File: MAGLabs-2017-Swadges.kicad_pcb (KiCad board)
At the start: 2 copper layers, 70 x 120 mm, 34 parts, among them J1 LCD Screen, J2 Valve Magic, J3 Program, U1 ESP12E

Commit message: Update Swadges design
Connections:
- D2 pad 1: Net-(D2-Pad1) -> (no net)
- D7 pad 2: Net-(D7-Pad2) -> (no net)
- D8 pad 2: Net-(D8-Pad2) -> (no net)
- R2 pad 2: Net-(R2-Pad2) -> (no net)
- R3 pad 2: Net-(R3-Pad2) -> (no net)
- U1 pad 10: Net-(U1-Pad10) -> (no net)
- U1 pad 11: Net-(U1-Pad11) -> (no net)
- U1 pad 12: Net-(U1-Pad12) -> (no net)
- U1 pad 13: Net-(U1-Pad13) -> (no net)
- U1 pad 14: Net-(U1-Pad14) -> (no net)
- U1 pad 9: Net-(U1-Pad9) -> (no net)
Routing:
- net GND: track 0.00 -> 126.5 mm, vias 0 -> 15
- net +3V3: track 307.6 -> 309.2 mm, vias 0 -> 2
- net Net-(BT1-Pad2): track 81.6 -> 81.7 mm, vias 0 -> 4

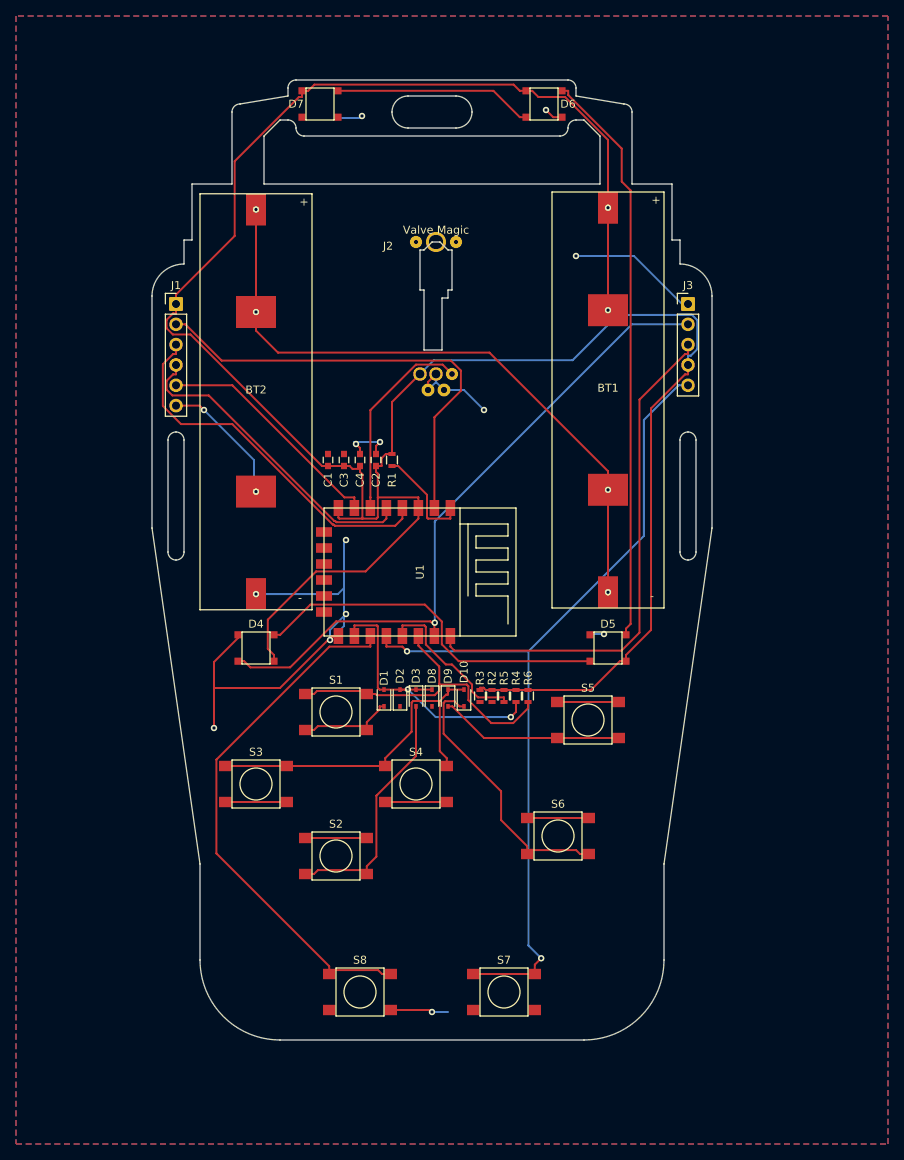
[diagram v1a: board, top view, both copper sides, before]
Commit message: Cleanup outputs
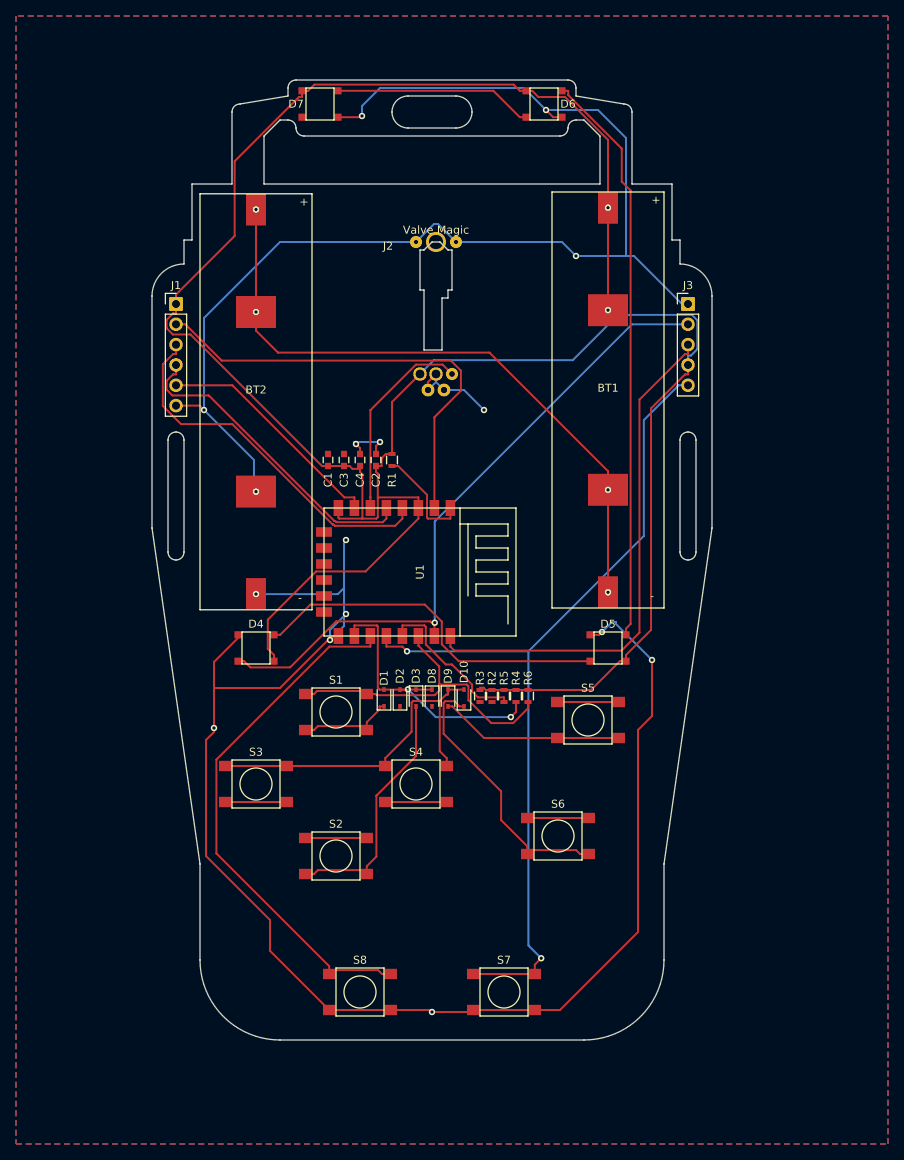
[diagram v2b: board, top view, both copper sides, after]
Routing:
- net GND: track 126.5 -> 366.9 mm, vias 15 -> 16
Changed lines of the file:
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@@
     (thickness 1.6)
     (drawings 74)
-    (tracks 383)
+    (tracks 419)
     (zones 0)
     (modules 34)
@@
   (segment (start 168 70.62) (end 168 71.7953) (width 0.25) (layer F.Cu) (net 2))
   (segment (start 160.25 107.65) (end 160.25 106.8747) (width 0.25) (layer F.Cu) (net 2))
-  (segment (start 152.25 39.65) (end 151.15 39.65) (width 0.25) (layer F.Cu) (net 3) (status 400000))
+  (segment (start 107.5 76.25) (end 107.5 64.75) (width 0.25) (layer B.Cu) (net 3))
+  (segment (start 117 55.25) (end 134 55.25) (width 0.25) (layer B.Cu) (net 3) (status 800000))
+  (segment (start 107.5 64.75) (end 117 55.25) (width 0.25) (layer B.Cu) (net 3))
+  (segment (start 139 55.25) (end 136.75 53) (width 0.25) (layer B.Cu) (net 3) (status 400000))
+  (segment (start 136.75 53) (end 136.25 53) (width 0.25) (layer B.Cu) (net 3))
+  (segment (start 136.25 53) (end 134 55.25) (width 0.25) (layer B.Cu) (net 3) (status 800000))
+  (segment (start 139 55.25) (end 152.25 55.25) (width 0.25) (layer B.Cu) (net 3) (status 400000))
+  (via (at 154 57) (size 0.8) (drill 0.4) (layers F.Cu B.Cu) (net 3))
+  (segment (start 154 57) (end 160.25 57) (width 0.25) (layer B.Cu) (net 3))
+  (segment (start 152.25 55.25) (end 154 57) (width 0.25) (layer B.Cu) (net 3))
+  (segment (start 150.25 38.75) (end 156.75 38.75) (width 0.25) (layer B.Cu) (net 3))
+  (segment (start 160.25 42.25) (end 160.25 57) (width 0.25) (layer B.Cu) (net 3))
+  (segment (start 156.75 38.75) (end 160.25 42.25) (width 0.25) (layer B.Cu) (net 3))
+  (segment (start 127.25 39.5) (end 127.25 38.25) (width 0.25) (layer B.Cu) (net 3))
+  (via (at 150.25 38.75) (size 0.8) (drill 0.4) (layers F.Cu B.Cu) (net 3))
   (segment (start 151.15 39.65) (end 150.25 38.75) (width 0.25) (layer F.Cu) (net 3))
-  (via (at 150.25 38.75) (size 0.8) (drill 0.4) (layers F.Cu B.Cu) (net 3))
-  (segment (start 124.5 39.75) (end 127 39.75) (width 0.25) (layer B.Cu) (net 3))
-  (segment (start 127 39.75) (end 127.25 39.5) (width 0.25) (layer B.Cu) (net 3))
+  (segment (start 152.25 39.65) (end 151.15 39.65) (width 0.25) (layer F.Cu) (net 3))
+  (segment (start 127.1 39.65) (end 127.25 39.5) (width 0.25) (layer F.Cu) (net 3))
   (via (at 127.25 39.5) (size 0.8) (drill 0.4) (layers F.Cu B.Cu) (net 3))
-  (segment (start 156 104.25) (end 157.5 104.25) (width 0.25) (layer B.Cu) (net 3))
-  (via (at 157.5 104.25) (size 0.8) (drill 0.4) (layers F.Cu B.Cu) (net 3))
-  (segment (start 157.5 104.25) (end 157.75 104.25) (width 0.25) (layer F.Cu) (net 3))
-  (segment (start 168 63) (end 167.25 63) (width 0.25) (layer B.Cu) (net 3) (status C00000))
-  (segment (start 167.25 63) (end 161.25 57) (width 0.25) (layer B.Cu) (net 3) (status 400000))
-  (segment (start 161.25 57) (end 154 57) (width 0.25) (layer B.Cu) (net 3))
-  (via (at 154 57) (size 0.8) (drill 0.4) (layers F.Cu B.Cu) (net 3))
-  (segment (start 104 75.7) (end 106.95 75.7) (width 0.25) (layer F.Cu) (net 3) (status 400000))
+  (segment (start 127.1 39.65) (end 124.25 39.65) (width 0.25) (layer F.Cu) (net 3) (status 800000))
+  (segment (start 147.5 36) (end 150.25 38.75) (width 0.25) (layer B.Cu) (net 3))
+  (segment (start 129.5 36) (end 147.5 36) (width 0.25) (layer B.Cu) (net 3))
+  (segment (start 127.25 38.25) (end 129.5 36) (width 0.25) (layer B.Cu) (net 3))
+  (segment (start 108.75 116) (end 108.75 116.5) (width 0.25) (layer F.Cu) (net 3))
+  (via (at 108.75 116) (size 0.8) (drill 0.4) (layers F.Cu B.Cu) (net 3))
+  (segment (start 108.75 111) (end 108.75 116) (width 0.25) (layer F.Cu) (net 3))
+  (segment (start 115.75 143.85) (end 123.15 151.25) (width 0.25) (layer F.Cu) (net 3) (status 800000))
+  (segment (start 115.75 140) (end 115.75 143.85) (width 0.25) (layer F.Cu) (net 3))
+  (segment (start 107.75 132) (end 115.75 140) (width 0.25) (layer F.Cu) (net 3))
+  (segment (start 107.75 117.5) (end 107.75 132) (width 0.25) (layer F.Cu) (net 3))
+  (segment (start 108.75 116.5) (end 107.75 117.5) (width 0.25) (layer F.Cu) (net 3))
+  (segment (start 159 102.75) (end 158.5 102.75) (width 0.25) (layer B.Cu) (net 3))
+  (segment (start 152 151.25) (end 161.75 141.5) (width 0.25) (layer F.Cu) (net 3))
+  (segment (start 161.75 141.5) (end 161.75 116.25) (width 0.25) (layer F.Cu) (net 3))
+  (segment (start 161.75 116.25) (end 163.5 114.5) (width 0.25) (layer F.Cu) (net 3))
+  (segment (start 163.5 114.5) (end 163.5 107.5) (width 0.25) (layer F.Cu) (net 3))
+  (via (at 163.5 107.5) (size 0.8) (drill 0.4) (layers F.Cu B.Cu) (net 3))
+  (segment (start 163.5 107.5) (end 159 103) (width 0.25) (layer B.Cu) (net 3))
+  (segment (start 159 103) (end 159 102.75) (width 0.25) (layer B.Cu) (net 3))
+  (segment (start 148.85 151.25) (end 152 151.25) (width 0.25) (layer F.Cu) (net 3) (status 400000))
+  (segment (start 156.9 104.35) (end 155.75 104.35) (width 0.25) (layer F.Cu) (net 3) (status 800000))
+  (segment (start 157.25 104) (end 156.9 104.35) (width 0.25) (layer F.Cu) (net 3))
+  (via (at 157.25 104) (size 0.8) (drill 0.4) (layers F.Cu B.Cu) (net 3))
+  (segment (start 158.5 102.75) (end 157.25 104) (width 0.25) (layer B.Cu) (net 3))
+  (segment (start 141.15 151.25) (end 148.85 151.25) (width 0.25) (layer F.Cu) (net 3) (status C00000))
+  (segment (start 136 151.5) (end 140.9 151.5) (width 0.25) (layer F.Cu) (net 3) (status 800000))
+  (segment (start 140.9 151.5) (end 141.15 151.25) (width 0.25) (layer F.Cu) (net 3) (status C00000))
+  (segment (start 123.15 151.25) (end 130.85 151.25) (width 0.25) (layer F.Cu) (net 3) (status C00000))
+  (segment (start 168 63) (end 167.25 63) (width 0.25) (layer B.Cu) (net 3))
+  (segment (start 167.25 63) (end 161.25 57) (width 0.25) (layer B.Cu) (net 3))
+  (segment (start 161.25 57) (end 160.25 57) (width 0.25) (layer B.Cu) (net 3))
+  (segment (start 104 75.7) (end 106.95 75.7) (width 0.25) (layer F.Cu) (net 3))
   (segment (start 106.95 75.7) (end 107.5 76.25) (width 0.25) (layer F.Cu) (net 3))
   (via (at 107.5 76.25) (size 0.8) (drill 0.4) (layers F.Cu B.Cu) (net 3))
   (segment (start 107.5 76.25) (end 113.75 82.5) (width 0.25) (layer B.Cu) (net 3))
   (segment (start 113.75 82.5) (end 113.75 85.5) (width 0.25) (layer B.Cu) (net 3))
-  (segment (start 137.5 73.75) (end 140 73.75) (width 0.25) (layer B.Cu) (net 3) (status 400000))
+  (segment (start 137.5 73.75) (end 140 73.75) (width 0.25) (layer B.Cu) (net 3))
   (segment (start 140 73.75) (end 142.5 76.25) (width 0.25) (layer B.Cu) (net 3))
   (via (at 142.5 76.25) (size 0.8) (drill 0.4) (layers F.Cu B.Cu) (net 3))
@@
   (segment (start 125 92.75) (end 125.25 92.5) (width 0.25) (layer B.Cu) (net 3))
   (via (at 125.25 92.5) (size 0.8) (drill 0.4) (layers F.Cu B.Cu) (net 3))
-  (segment (start 124.3 104.5) (end 123.75 104.5) (width 0.25) (layer F.Cu) (net 3) (status C00000))
-  (segment (start 123.75 104.5) (end 123.25 105) (width 0.25) (layer F.Cu) (net 3) (status 400000))
+  (segment (start 124.3 104.5) (end 123.75 104.5) (width 0.25) (layer F.Cu) (net 3))
+  (segment (start 123.75 104.5) (end 123.25 105) (width 0.25) (layer F.Cu) (net 3))
   (via (at 123.25 105) (size 0.8) (drill 0.4) (layers F.Cu B.Cu) (net 3))
   (segment (start 123.25 105) (end 125 103.25) (width 0.25) (layer B.Cu) (net 3))
@@
   (segment (start 125 98.5) (end 124.24 99.26) (width 0.25) (layer B.Cu) (net 3))
   (segment (start 124.24 99.26) (end 114 99.26) (width 0.25) (layer B.Cu) (net 3))
-  (segment (start 124.3 104.5) (end 123.5 104.5) (width 0.25) (layer F.Cu) (net 3) (status 400000))
+  (segment (start 124.3 104.5) (end 123.5 104.5) (width 0.25) (layer F.Cu) (net 3))
   (segment (start 123.5 104.5) (end 117 111) (width 0.25) (layer F.Cu) (net 3))
   (segment (start 117 111) (end 108.75 111) (width 0.25) (layer F.Cu) (net 3))
-  (segment (start 136.5 71.75) (end 136.5 72.75) (width 0.25) (layer B.Cu) (net 3) (status 400000))
-  (segment (start 136.5 72.75) (end 135.5 73.75) (width 0.25) (layer B.Cu) (net 3) (status 800000))
-  (segment (start 136.5 72.75) (end 137.5 73.75) (width 0.25) (layer B.Cu) (net 3) (status 800000))
-  (segment (start 135.5 73.75) (end 135.5 72.75) (width 0.25) (layer F.Cu) (net 3) (status 400000))
-  (segment (start 135.5 72.75) (end 136.5 71.75) (width 0.25) (layer F.Cu) (net 3) (status 800000))
-  (segment (start 129 81.75) (end 129 80.75) (width 0.25) (layer F.Cu) (net 3) (status 400000))
-  (segment (start 127 81) (end 127 81.75) (width 0.25) (layer F.Cu) (net 3) (status 800000))
+  (segment (start 136.5 71.75) (end 136.5 72.75) (width 0.25) (layer B.Cu) (net 3))
+  (segment (start 136.5 72.75) (end 135.5 73.75) (width 0.25) (layer B.Cu) (net 3))
+  (segment (start 136.5 72.75) (end 137.5 73.75) (width 0.25) (layer B.Cu) (net 3))
+  (segment (start 135.5 73.75) (end 135.5 72.75) (width 0.25) (layer F.Cu) (net 3))
+  (segment (start 135.5 72.75) (end 136.5 71.75) (width 0.25) (layer F.Cu) (net 3))
+  (segment (start 129 81.75) (end 129 80.75) (width 0.25) (layer F.Cu) (net 3))
+  (segment (start 127 81) (end 127 81.75) (width 0.25) (layer F.Cu) (net 3))
   (segment (start 126.5 80.5) (end 127 81) (width 0.25) (layer F.Cu) (net 3))
   (via (at 126.5 80.5) (size 0.8) (drill 0.4) (layers F.Cu B.Cu) (net 3))
@@
   (segment (start 111.75 104.75) (end 108.75 107.75) (width 0.25) (layer F.Cu) (net 3))
   (segment (start 108.75 107.75) (end 108.75 111) (width 0.25) (layer F.Cu) (net 3))
-  (segment (start 108.75 111) (end 108.75 116) (width 0.25) (layer F.Cu) (net 3))
-  (via (at 108.75 116) (size 0.8) (drill 0.4) (layers F.Cu B.Cu) (net 3))
   (via (at 114 86.45) (size 0.8) (drill 0.4) (layers F.Cu B.Cu) (net 3))
   (segment (start 114 86.45) (end 114 86.5) (width 0.25) (layer B.Cu) (net 3))
